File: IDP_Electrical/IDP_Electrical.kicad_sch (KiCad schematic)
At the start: 0 parts

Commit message: Updated schematic
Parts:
- added A1: PicoBot, symbol IDP_sample:PicoBot
- added Chip1: Optocoupler_ACPL-847-000E, symbol IDP_sample:Optocoupler_DC_PhotoNPN_AKEC
- added D1: Green LED, symbol Device:LED
- added D2: Red LED, symbol Device:LED
- added D3: Yellow LED, symbol Device:LED
- added D4: Blue LED, symbol Device:LED
- added M1, M2: DC Motor Symbol, symbol IDP_sample:DC Motor Symbol
- added PushButton1: ~, symbol IDP_sample:Push_Button
- added Resistor1, Resistor2, Resistor3: Test, symbol IDP:Resistor
- added Sensor1, Sensor2, Sensor3, Sensor4: SEN0017, symbol IDP_sample:Line_Sensor
- added Sensor5, Sensor6, Sensor7: TMF8701, symbol IDP_sample:TMF8701_Distance_Sensor
- added U1, U2: SER0038, symbol IDP:Standard_Servo Graphic
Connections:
- new net: A1.3 (Motor_3_12V), U2.1 (GND)
- new net: A1.2 (Motor_4_12V), U2.2 (Power_VCC)
- new net: A1.1 (Motor_1_6V5), A1.17 (GPIO13_and_Servo_2_PWM), U2.3 (PWM)
- new net: A1.3 (Motor_3_12V), U1.1 (GND)
- new net: A1.2 (Motor_4_12V), U1.2 (Power_VCC)
- new net: A1.1 (Motor_1_6V5), A1.20 (GPIO15_and_Servo_1_PWM), U1.3 (PWM)
- new net: Chip1.8, D3.1 (K)
- new net: D3.2 (A), Resistor3.1
- new net: A1.11 (GPIO8), Sensor5.1 (Data_Green), Sensor6.1 (Data_Green), Sensor7.1 (Data_Green)
- new net: A1.12 (GPIO9), Sensor5.2 (Clock_Blue), Sensor6.2 (Clock_Blue), Sensor7.2 (Clock_Blue)
- new net: A1.8 (GND), Sensor5.3 (GND_Black), Sensor6.3 (GND_Black), Sensor7.3 (GND_Black)
- new net: A1.36 (From_Internal_Supply_3V3), D4.2 (A), PushButton1.2 (3V3_Power), Resistor1.2, Resistor2.2, Resistor3.2, Sensor1.2 (3V3_Power_Red), Sensor2.2 (3V3_Power_Red), Sensor3.2 (3V3_Power_Red), Sensor4.2 (3V3_Power_Red), Sensor5.4 (3V3_Power_Red), Sensor6.4 (3V3_Power_Red), Sensor7.4 (3V3_Power_Red)
- new net: A1.22 (GPIO17), Sensor3.1 (Output_Green)
- new net: A1.22 (GPIO17), Sensor1.3 (GND_Black), Sensor2.3 (GND_Black), Sensor3.3 (GND_Black), Sensor4.3 (GND_Black)
- new net: D1.2 (A), Resistor1.1
- new net: A1.25 (GPIO19), Sensor1.1 (Output_Green)
- new net: Chip1.8, D2.1 (K)
- new net: D2.2 (A), Resistor2.1
- new net: A1.14 (GPIO10), Chip1.1
- new net: A1.16 (GPIO12), Chip1.1
- new net: A1.19 (GPIO14), Chip1.1
- new net: A1.3 (Motor_3_12V), Chip1.15, Chip1.2, Chip1.3, Chip1.7
- new net: Chip1.16, D1.1 (K)
- new net: A1.15 (GPIO11), Chip1.3
- new net: Chip1.8, D4.1 (K)
- new net: A1.2 (Motor_4_12V), M2.1 (+)
- new net: A1.2 (Motor_4_12V), M2.2 (-)
- new net: A1.21 (GPIO16), Sensor4.1 (Output_Green)
- new net: A1.24 (GPIO18), Sensor2.1 (Output_Green)
- new net: A1.3 (Motor_3_12V), M1.1 (+)
- new net: A1.2 (Motor_4_12V), M1.2 (-)
- new net: A1.29 (GPIO22), PushButton1.1 (Data)
- new net: A1.38 (GND), PushButton1.3 (GND)
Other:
- note added: "150"

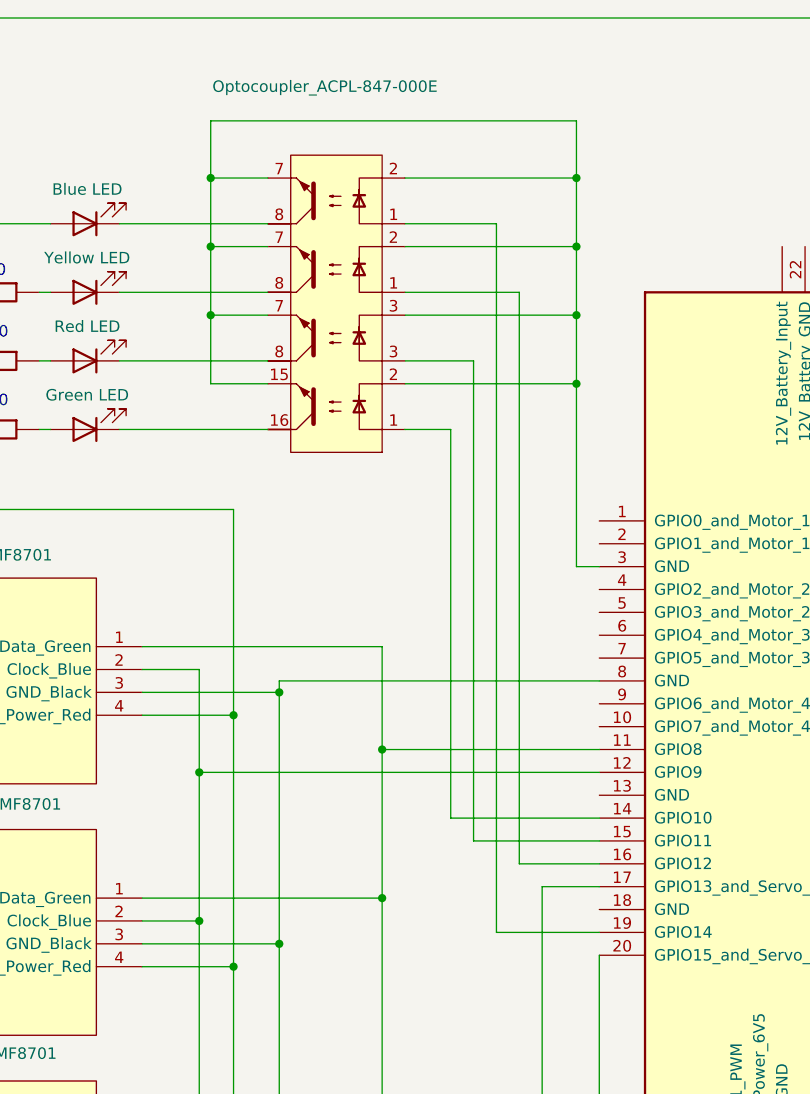
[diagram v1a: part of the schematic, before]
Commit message: added 480 ohmn R to optocoupler
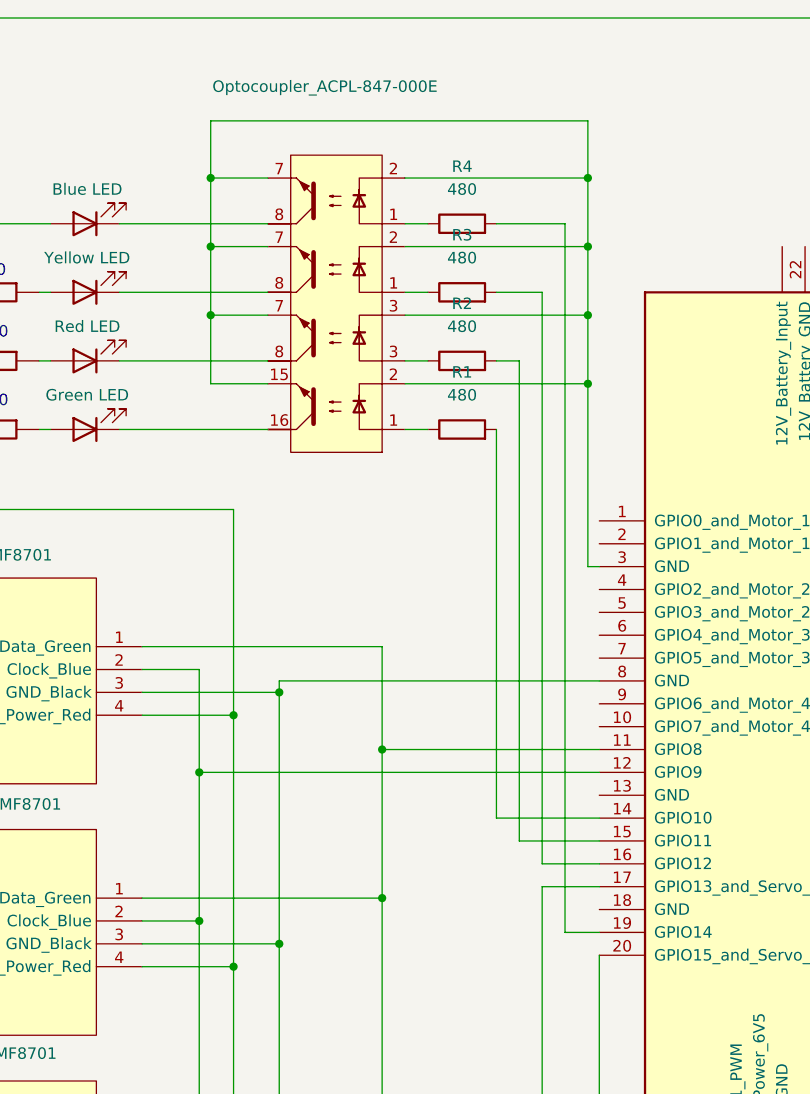
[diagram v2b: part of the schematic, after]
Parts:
- added R1, R2, R3, R4: 480, symbol Device:R
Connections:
- net at A1.14 (GPIO10): now also R1.2; no longer Chip1.1
- net at A1.16 (GPIO12): now also R3.2; no longer Chip1.1
- net at Chip1.1: now also R4.1; no longer A1.19 (GPIO14)
- net at Chip1.3: now also R2.1; no longer A1.15 (GPIO11)
- new net: Chip1.1, R3.1
- new net: Chip1.1, R1.1
- new net: A1.15 (GPIO11), R2.2
- new net: A1.19 (GPIO14), R4.2

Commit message: Footnote assigned in Schematics and PCB generated (with warnings)
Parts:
- A1: footprint (none) -> Connector_PinSocket_2.54mm:PinSocket_2x20_P2.54mm_Vertical
- Chip1: footprint (none) -> Package_DIP:DIP-16_W7.62mm
- D1, D2, D3, D4: footprint (none) -> LED_THT:LED_D5.0mm
- M1, M2: footprint (none) -> TerminalBlock_CUI:TerminalBlock_CUI_TB007-508-02_1x02_P5.08mm_Horizontal
- PushButton1, Sensor1, Sensor2, Sensor3, Sensor4, U1, U2: footprint (none) -> Connector_PinHeader_2.54mm:PinHeader_1x03_P2.54mm_Vertical
- R1, R2, R3, R4, Resistor1, Resistor2, Resistor3: footprint (none) -> Resistor_THT:R_Axial_DIN0207_L6.3mm_D2.5mm_P7.62mm_Horizontal
- Sensor5, Sensor6, Sensor7: footprint (none) -> Connector_PinHeader_2.54mm:PinHeader_1x04_P2.54mm_Vertical
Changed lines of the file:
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@@
 			)
 		)
-		(property "Footprint" ""
+		(property "Footprint" "Connector_PinHeader_2.54mm:PinHeader_1x03_P2.54mm_Vertical"
 			(at 20.32 173.99 0)
 			(effects
@@
 			)
 		)
-		(property "Footprint" ""
+		(property "Footprint" "Connector_PinHeader_2.54mm:PinHeader_1x03_P2.54mm_Vertical"
 			(at 68.58 175.26 0)
 			(effects
@@
 			)
 		)
-		(property "Footprint" ""
+		(property "Footprint" "Resistor_THT:R_Axial_DIN0207_L6.3mm_D2.5mm_P7.62mm_Horizontal"
 			(at 77.47 48.768 90)
 			(effects
@@
 			)
 		)
-		(property "Footprint" ""
+		(property "Footprint" "LED_THT:LED_D5.0mm"
 			(at 35.56 46.99 0)
 			(effects
@@
 			)
 		)
-		(property "Footprint" ""
+		(property "Footprint" "Connector_PinHeader_2.54mm:PinHeader_1x04_P2.54mm_Vertical"
 			(at 31.75 147.32 0)
 			(effects
@@
 			)
 		)
-		(property "Footprint" ""
+		(property "Footprint" "Connector_PinHeader_2.54mm:PinHeader_1x03_P2.54mm_Vertical"
 			(at 232.41 95.25 0)
 			(effects
@@
 			)
 		)
-		(property "Footprint" ""
+		(property "Footprint" "Resistor_THT:R_Axial_DIN0207_L6.3mm_D2.5mm_P7.62mm_Horizontal"
 			(at 22.86 60.452 90)
 			(effects
@@
 			)
 		)
-		(property "Footprint" ""
+		(property "Footprint" "Connector_PinHeader_2.54mm:PinHeader_1x03_P2.54mm_Vertical"
 			(at 232.41 60.96 0)
 			(effects
@@
 			)
 		)
-		(property "Footprint" ""
+		(property "Footprint" "Resistor_THT:R_Axial_DIN0207_L6.3mm_D2.5mm_P7.62mm_Horizontal"
 			(at 22.86 45.212 90)
 			(effects
@@
 			)
 		)
-		(property "Footprint" ""
+		(property "Footprint" "LED_THT:LED_D5.0mm"
 			(at 35.56 54.61 0)
 			(effects
@@
 			)
 		)
-		(property "Footprint" ""
+		(property "Footprint" "Resistor_THT:R_Axial_DIN0207_L6.3mm_D2.5mm_P7.62mm_Horizontal"
 			(at 77.47 64.008 90)
 			(effects
@@
 			)
 		)
-		(property "Footprint" ""
+		(property "Footprint" "Resistor_THT:R_Axial_DIN0207_L6.3mm_D2.5mm_P7.62mm_Horizontal"
 			(at 22.86 52.832 90)
 			(effects
@@
 			)
 		)
-		(property "Footprint" ""
+		(property "Footprint" "Package_DIP:DIP-16_W7.62mm"
 			(at 68.58 44.45 0)
 			(effects
@@
 			)
 		)
-		(property "Footprint" ""
+		(property "Footprint" "Resistor_THT:R_Axial_DIN0207_L6.3mm_D2.5mm_P7.62mm_Horizontal"
 			(at 77.47 56.388 90)
 			(effects
@@
 			)
 		)
-		(property "Footprint" ""
+		(property "Footprint" "Connector_PinHeader_2.54mm:PinHeader_1x04_P2.54mm_Vertical"
 			(at 31.75 119.38 0)
 			(effects
@@
 			)
 		)
-		(property "Footprint" ""
+		(property "Footprint" "TerminalBlock_CUI:TerminalBlock_CUI_TB007-508-02_1x02_P5.08mm_Horizontal"
 			(at 161.544 168.91 0)
 			(effects
@@
 			)
 		)
-		(property "Footprint" ""
+		(property "Footprint" "Connector_PinHeader_2.54mm:PinHeader_1x03_P2.54mm_Vertical"
 			(at 232.41 110.49 0)
 			(effects
@@
 			)
 		)
-		(property "Footprint" ""
+		(property "Footprint" "LED_THT:LED_D5.0mm"
 			(at 35.56 62.23 0)
 			(effects
@@
 			)
 		)
-		(property "Footprint" ""
+		(property "Footprint" "Connector_PinHeader_2.54mm:PinHeader_1x03_P2.54mm_Vertical"
 			(at 232.41 78.74 0)
 			(effects
@@
 			)
 		)
-		(property "Footprint" ""
+		(property "Footprint" "Resistor_THT:R_Axial_DIN0207_L6.3mm_D2.5mm_P7.62mm_Horizontal"
 			(at 77.47 41.148 90)
 			(effects
@@
 			)
 		)
-		(property "Footprint" ""
+		(property "Footprint" "Connector_PinHeader_2.54mm:PinHeader_1x04_P2.54mm_Vertical"
 			(at 31.75 91.44 0)
 			(effects
@@
 			)
 		)
-		(property "Footprint" ""
+		(property "Footprint" "LED_THT:LED_D5.0mm"
 			(at 35.56 39.37 0)
 			(effects
@@
 			)
 		)
-		(property "Footprint" ""
+		(property "Footprint" "TerminalBlock_CUI:TerminalBlock_CUI_TB007-508-02_1x02_P5.08mm_Horizontal"
 			(at 138.684 168.91 0)
 			(effects
@@
 			)
 		)
-		(property "Footprint" ""
+		(property "Footprint" "Connector_PinHeader_2.54mm:PinHeader_1x03_P2.54mm_Vertical"
 			(at 201.93 36.83 0)
 			(effects
@@
 		(exclude_from_sim no)
 		(in_bom yes)
-		(on_board yes)
+		(on_board no)
 		(dnp no)
 		(fields_autoplaced yes)
@@
 			)
 		)
-		(property "Footprint" ""
+		(property "Footprint" "Connector_PinSocket_2.54mm:PinSocket_2x20_P2.54mm_Vertical"
 			(at 133.35 168.91 0)
 			(effects

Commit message: added US, LED GPIO correction
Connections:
- net at R1.2: now also A1.19 (GPIO14); no longer A1.14 (GPIO10)
- net at R4.2: now also A1.14 (GPIO10); no longer A1.19 (GPIO14)
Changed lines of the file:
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@@
-	(wire
-		(pts
-			(xy 92.71 118.11) (xy 88.9 118.11)
-		)
-		(stroke
-			(width 0)
-			(type default)
-		)
-	)
 	(wire
 		(pts
@@
 	(wire
 		(pts
-			(xy 92.71 105.41) (xy 81.28 105.41)
-		)
-		(stroke
-			(width 0)
-			(type default)
-		)
-	)
-	(wire
-		(pts
 			(xy 176.53 34.29) (xy 176.53 100.33)
 		)
@@
 	(wire
 		(pts
+			(xy 88.9 105.41) (xy 92.71 105.41)
+		)
+		(stroke
+			(width 0)
+			(type default)
+		)
+	)
+	(wire
+		(pts
 			(xy 41.91 88.9) (xy 48.26 88.9)
 		)
@@
 	(wire
 		(pts
+			(xy 81.28 62.23) (xy 81.28 118.11)
+		)
+		(stroke
+			(width 0)
+			(type default)
+		)
+	)
+	(wire
+		(pts
 			(xy 177.8 120.65) (xy 177.8 107.95)
 		)
@@
 	(wire
 		(pts
-			(xy 81.28 105.41) (xy 81.28 62.23)
-		)
-		(stroke
-			(width 0)
-			(type default)
-		)
-	)
-	(wire
-		(pts
 			(xy 168.91 82.55) (xy 171.45 82.55)
 		)
@@
 	(wire
 		(pts
+			(xy 81.28 118.11) (xy 92.71 118.11)
+		)
+		(stroke
+			(width 0)
+			(type default)
+		)
+	)
+	(wire
+		(pts
 			(xy 212.09 63.5) (xy 199.39 63.5)
 		)
@@
 	(wire
 		(pts
+			(xy 88.9 39.37) (xy 88.9 105.41)
+		)
+		(stroke
+			(width 0)
+			(type default)
+		)
+	)
+	(wire
+		(pts
 			(xy 83.82 54.61) (xy 81.28 54.61)
 		)
@@
 		)
 		(stroke
-			(width 0)
-			(type default)
-		)
-	)
-	(wire
-		(pts
-			(xy 88.9 39.37) (xy 88.9 118.11)
-		)
-		(stroke

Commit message: Added US, updated LED GPIO
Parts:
- added SEN1: ~, symbol IDP_sample:Ultrasonic_Distance_Sensor
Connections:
- net at R3.2: now also A1.15 (GPIO11); no longer A1.16 (GPIO12)
- net at A1.36 (From_Internal_Supply_3V3), D4.2 (A), PushButton1.2 (3V3_Power)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: now also SEN1.2 (3V3_Red)
- net at A1.22 (GPIO17), Sensor1.3 (GND_Black), Sensor2.3 (GND_Black)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: now also SEN1.1 (GND_Black)
- net at R1.2: now also A1.14 (GPIO10); no longer A1.19 (GPIO14)
- net at R2.2: now also A1.16 (GPIO12); no longer A1.15 (GPIO11)
- net at R4.2: now also A1.19 (GPIO14); no longer A1.14 (GPIO10)
- net at A1.27 (GPIO21): now also SEN1.3 (Analog_Ouput_Blue)
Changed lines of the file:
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@@
 	)
 	(junction
+		(at 199.39 115.57)
+		(diameter 0)
+		(color 0 0 0 0)
+	)
+	(junction
 		(at 68.58 97.79)
 		(diameter 0)
@@
 	)
 	(junction
+		(at 195.58 110.49)
+		(diameter 0)
+		(color 0 0 0 0)
+	)
+	(junction
 		(at 57.15 119.38)
 		(diameter 0)
@@
 	(wire
 		(pts
+			(xy 86.36 107.95) (xy 86.36 46.99)
+		)
+		(stroke
+			(width 0)
+			(type default)
+		)
+	)
+	(wire
+		(pts
 			(xy 41.91 119.38) (xy 57.15 119.38)
 		)
@@
 	(wire
 		(pts
+			(xy 195.58 120.65) (xy 205.74 120.65)
+		)
+		(stroke
+			(width 0)
+			(type default)
+		)
+	)
+	(wire
+		(pts
 			(xy 118.11 154.94) (xy 118.11 148.59)
 		)
@@
 	(wire
 		(pts
+			(xy 83.82 54.61) (xy 83.82 110.49)
+		)
+		(stroke
+			(width 0)
+			(type default)
+		)
+	)
+	(wire
+		(pts
 			(xy 55.88 57.15) (xy 49.53 57.15)
 		)
@@
 	(wire
 		(pts
+			(xy 88.9 39.37) (xy 88.9 118.11)
+		)
+		(stroke
+			(width 0)
+			(type default)
+		)
+	)
+	(wire
+		(pts
+			(xy 168.91 105.41) (xy 187.96 105.41)
+		)
+		(stroke
+			(width 0)
+			(type default)
+		)
+	)
+	(wire
+		(pts
+			(xy 86.36 107.95) (xy 92.71 107.95)
+		)
+		(stroke
+			(width 0)
+			(type default)
+		)
+	)
+	(wire
+		(pts
 			(xy 171.45 60.96) (xy 171.45 36.83)
 		)
@@
 	(wire
 		(pts
-			(xy 83.82 107.95) (xy 83.82 54.61)
+			(xy 83.82 110.49) (xy 92.71 110.49)
 		)
 		(stroke
@@
 	(wire
 		(pts
+			(xy 195.58 110.49) (xy 195.58 120.65)
+		)
+		(stroke
+			(width 0)
+			(type default)
+		)
+	)
+	(wire
+		(pts
 			(xy 172.72 92.71) (xy 212.09 92.71)
 		)
@@
 	(wire
 		(pts
-			(xy 92.71 107.95) (xy 83.82 107.95)
+			(xy 52.07 93.98) (xy 52.07 121.92)
 		)
 		(stroke
@@
 	(wire
 		(pts
-			(xy 52.07 93.98) (xy 52.07 121.92)
+			(xy 176.53 34.29) (xy 176.53 100.33)
 		)
 		(stroke
@@
 	(wire
 		(pts
-			(xy 176.53 34.29) (xy 176.53 100.33)
+			(xy 203.2 124.46) (xy 187.96 124.46)
 		)
 		(stroke
@@
 	(wire
 		(pts
+			(xy 203.2 129.54) (xy 203.2 124.46)
+		)
+		(stroke
+			(width 0)
+			(type default)
+		)
+	)
+	(wire
+		(pts
 			(xy 212.09 78.74) (xy 195.58 78.74)
 		)
@@
 	(wire
 		(pts
-			(xy 88.9 105.41) (xy 92.71 105.41)
+			(xy 41.91 88.9) (xy 48.26 88.9)
 		)
 		(stroke
@@
 	(wire
 		(pts
-			(xy 41.91 88.9) (xy 48.26 88.9)
+			(xy 208.28 115.57) (xy 208.28 129.54)
 		)
 		(stroke
@@
 	(wire
 		(pts
-			(xy 81.28 62.23) (xy 81.28 118.11)
+			(xy 81.28 62.23) (xy 81.28 105.41)
 		)
 		(stroke
@@
 	(wire
 		(pts
-			(xy 171.45 36.83) (xy 171.45 16.51)
+			(xy 88.9 118.11) (xy 92.71 118.11)
 		)
 		(stroke
@@
 	(wire
 		(pts
-			(xy 177.8 107.95) (xy 212.09 107.95)
+			(xy 171.45 36.83) (xy 171.45 16.51)
 		)
 		(stroke
@@
 	(wire
 		(pts
-			(xy 92.71 120.65) (xy 92.71 149.86)
+			(xy 177.8 107.95) (xy 212.09 107.95)
 		)
 		(stroke
 			(width 0)
-			(type dash)
+			(type default)
 		)
 	)
 	(wire
 		(pts
-			(xy 86.36 154.94) (xy 118.11 154.94)
+			(xy 92.71 120.65) (xy 92.71 149.86)
 		)
 		(stroke
 			(width 0)
-			(type default)
+			(type dash)
 		)
 	)
 	(wire
 		(pts
-			(xy 173.99 39.37) (xy 173.99 77.47)
+			(xy 86.36 154.94) (xy 118.11 154.94)
 		)
 		(stroke
@@
 	(wire
 		(pts
-			(xy 92.71 110.49) (xy 86.36 110.49)
+			(xy 173.99 39.37) (xy 173.99 77.47)
 		)
 		(stroke
@@
 	(wire
 		(pts
-			(xy 68.58 97.79) (xy 92.71 97.79)
+			(xy 199.39 115.57) (xy 208.28 115.57)
 		)
 		(stroke
@@
 	(wire
 		(pts
-			(xy 53.34 186.69) (xy 57.15 186.69)
+			(xy 68.58 97.79) (xy 92.71 97.79)
 		)
 		(stroke
@@
 	(wire
 		(pts
-			(xy 199.39 113.03) (xy 199.39 115.57)
+			(xy 53.34 186.69) (xy 57.15 186.69)
 		)
 		(stroke
@@
 	(wire
 		(pts
-			(xy 53.34 181.61) (xy 62.23 181.61)
+			(xy 199.39 113.03) (xy 199.39 115.57)
 		)
 		(stroke
@@
 	(wire
 		(pts
-			(xy 41.91 93.98) (xy 52.07 93.98)
+			(xy 53.34 181.61) (xy 62.23 181.61)
 		)
 		(stroke
@@
 	(wire
 		(pts
-			(xy 52.07 149.86) (xy 41.91 149.86)
+			(xy 41.91 93.98) (xy 52.07 93.98)
 		)
 		(stroke
@@
 	(wire
 		(pts
-			(xy 52.07 71.12) (xy 52.07 93.98)
+			(xy 52.07 149.86) (xy 41.91 149.86)
 		)
 		(stroke
@@
 	(wire
 		(pts
-			(xy 81.28 118.11) (xy 92.71 118.11)
+			(xy 52.07 71.12) (xy 52.07 93.98)
 		)
 		(stroke
@@
 	(wire
 		(pts
-			(xy 88.9 39.37) (xy 88.9 105.41)
-		)
-		(stroke
-			(width 0)
-			(type default)
-		)
-	)
-	(wire
-		(pts
 			(xy 83.82 54.61) (xy 81.28 54.61)
 		)
@@
 	(wire
 		(pts
-			(xy 120.65 157.48) (xy 120.65 148.59)
+			(xy 205.74 120.65) (xy 205.74 129.54)
 		)
 		(stroke
@@
 	(wire
 		(pts
-			(xy 195.58 110.49) (xy 195.58 95.25)
+			(xy 120.65 157.48) (xy 120.65 148.59)
 		)
 		(stroke
@@
 	(wire
 		(pts
-			(xy 41.91 142.24) (xy 68.58 142.24)
+			(xy 195.58 110.49) (xy 195.58 95.25)
 		)
 		(stroke
@@
 	(wire
 		(pts
-			(xy 86.36 110.49) (xy 86.36 46.99)
+			(xy 41.91 142.24) (xy 68.58 142.24)
 		)
 		(stroke
@@
 	(wire
 		(pts
+			(xy 187.96 124.46) (xy 187.96 105.41)
+		)
+		(stroke
+			(width 0)
+			(type default)
+		)
+	)
+	(wire
+		(pts
 			(xy 91.44 77.47) (xy 92.71 77.47)
 		)
@@
 	(wire
 		(pts
+			(xy 81.28 105.41) (xy 92.71 105.41)
+		)
+		(stroke
+			(width 0)
+			(type default)
+		)
+	)
+	(wire
+		(pts
 			(xy 181.61 34.29) (xy 176.53 34.29)
 		)
@@
 					(unit 1)
 				)
+			)
+		)
+	)
+	(symbol
+		(lib_id "IDP_sample:Ultrasonic_Distance_Sensor")
+		(at 208.28 139.7 180)
+		(unit 1)
+		(exclude_from_sim no)
+		(in_bom yes)
+		(on_board yes)
+		(dnp no)
+		(fields_autoplaced yes)
+		(property "Reference" "SEN1"
+			(at 205.74 147.32 0)
+			(effects
+				(font
+					(size 1.27 1.27)
+				)
+				(hide yes)
+			)
+		)
+		(property "Value" "~"
+			(at 229.87 142.2399 0)
+			(effects
+				(font
+					(size 1.27 1.27)
+				)
+				(justify right)
+			)
+		)
+		(property "Footprint" ""
+			(at 208.28 139.7 0)
+			(effects
+				(font
+					(size 1.27 1.27)
+				)
+				(hide yes)
+			)
+		)
+		(property "Datasheet" "https://www.dfrobot.com/product-1862.html"
+			(at 229.87 144.7799 0)
+			(effects
+				(font
+					(size 1.27 1.27)
+				)
+				(justify right)
+			)
+		)
+		(property "Description" "URM09 Ultrasonic Distance Sensor (2～500cm, Analog)"
+			(at 229.87 147.3199 0)
+			(effects
+				(font
+					(size 1.27 1.27)
+				)
+				(justify right)
+			)
+		)
+		(pin "1"
+		)
+		(pin "2"
+		)
+		(pin "3"
+		)
+		(instances
+			(project ""
+				(path "/ce89d3df-0ec9-4092-8b0c-885a49b1b5ae"
+					(reference "SEN1")
+					(unit 1)
+				)

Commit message: updated circuitry on R_test
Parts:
- added R5: 2.2k, symbol Device:R
- added R6: R_test, symbol Device:R
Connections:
- net at A1.36 (From_Internal_Supply_3V3), D4.2 (A), PushButton1.2 (3V3_Power)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: now also R6.2
- net at A1.22 (GPIO17), SEN1.1 (GND_Black), Sensor1.3 (GND_Black)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: now also R5.1
- net at A1.31 (GPIO26_ADC0): now also R5.2, R6.1

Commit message: updated PCB
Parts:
- R5, R6: footprint (none) -> Resistor_THT:R_Axial_DIN0207_L6.3mm_D2.5mm_P7.62mm_Horizontal
- SEN1: footprint (none) -> Connector_PinHeader_2.54mm:PinHeader_1x03_P2.54mm_Vertical
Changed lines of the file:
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@@
 			)
 		)
-		(property "Footprint" ""
+		(property "Footprint" "Resistor_THT:R_Axial_DIN0207_L6.3mm_D2.5mm_P7.62mm_Horizontal"
 			(at 226.06 130.048 90)
 			(effects
@@
 			)
 		)
-		(property "Footprint" ""
+		(property "Footprint" "Resistor_THT:R_Axial_DIN0207_L6.3mm_D2.5mm_P7.62mm_Horizontal"
 			(at 240.03 130.048 90)
 			(effects
@@
 			)
 		)
-		(property "Footprint" ""
+		(property "Footprint" "Connector_PinHeader_2.54mm:PinHeader_1x03_P2.54mm_Vertical"
 			(at 208.28 139.7 0)
 			(effects

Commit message: updated power and ground
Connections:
- net GND: now reaches R5.1, Sensor1.3 (GND_Black), Sensor2.3 (GND_Black), Sensor3.3 (GND_Black), Sensor4.3 (GND_Black)
- net GND: now also Chip1.15, Chip1.2, Chip1.3, Chip1.7, PushButton1.3 (GND), Sensor5.3 (GND_Black), Sensor6.3 (GND_Black), Sensor7.3 (GND_Black); no longer A1.22 (GPIO17), SEN1.1 (GND_Black)
- net at R5.2, R6.1: now also A1.32 (GPIO27_ADC1); no longer A1.31 (GPIO26_ADC0)
- net +3V3: now reaches D4.2 (A), PushButton1.2 (3V3_Power), R6.2, Resistor1.2, Resistor2.2, Resistor3.2, Sensor1.2 (3V3_Power_Red), Sensor2.2 (3V3_Power_Red), Sensor3.2 (3V3_Power_Red), Sensor4.2 (3V3_Power_Red), Sensor5.4 (3V3_Power_Red), Sensor6.4 (3V3_Power_Red), Sensor7.4 (3V3_Power_Red)
- net +3V3: no longer A1.36 (From_Internal_Supply_3V3), SEN1.2 (3V3_Red)
- net at A1.38 (GND): no longer PushButton1.3 (GND)
- now unconnected: A1.3 (Motor_3_12V), A1.8 (GND)
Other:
- moved on the sheet: M1, M2, PushButton1, R5, R6
